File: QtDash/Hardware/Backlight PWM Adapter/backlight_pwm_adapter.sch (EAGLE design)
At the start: 9 parts, among them Q1 310mA/60V/1.6Ω, Q2 310mA/60V/1.6Ω

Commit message: topic/backlight-pwm-control: 	- changed PWM frequency to 30kHz 	- renamed pwm.hpp -> pwm.h 	- started on rev b of PWM adapter board -- pwm signal used directly on EN pin of the OCX OC6700.  There is brightness control that is done outside of the backlight as well that I can't control with the PWM alone.
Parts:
- added C1: 100n, digital_dash:CL10B104MB8NNNC
- added C2: 1u, digital_dash:CL10A105KA8NNNC
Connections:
- net 5V: now also C1.1, C2.1
- net GND: now also C1.2, C2.2
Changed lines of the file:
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@@
 <setting verticaltext="up"/>
 </settings>
-<grid distance="0.1" unitdist="inch" unit="inch" style="lines" multiple="1" display="no" altdistance="0.01" altunitdist="inch" altunit="inch"/>
+<grid distance="0.05" unitdist="inch" unit="inch" style="lines" multiple="1" display="no" altdistance="0.01" altunitdist="inch" altunit="inch"/>
 <layers>
 <layer number="1" name="Top" color="4" fill="1" visible="no" active="no"/>
@@
 <part name="R3" library="digital_dash" deviceset="RC0603JR" device="" technology="-071KL" value="1k"/>
 <part name="GND4" library="SparkFun-PowerSymbols" deviceset="GND" device=""/>
+<part name="C1" library="digital_dash" deviceset="CL" device="" technology="10B104MB8NNNC" value="100n"/>
+<part name="C2" library="digital_dash" deviceset="CL" device="" technology="10A105KA8NNNC" value="1u"/>
+<part name="SUPPLY7" library="SparkFun-PowerSymbols" deviceset="5V" device=""/>
+<part name="GND5" library="SparkFun-PowerSymbols" deviceset="GND" device=""/>
 </parts>
 <sheets>
@@
 <instance part="R3" gate="G$1" x="50.8" y="30.48" rot="R180"/>
 <instance part="GND4" gate="1" x="40.64" y="22.86"/>
+<instance part="C1" gate="G$1" x="72.39" y="78.74"/>
+<instance part="C2" gate="G$1" x="64.77" y="78.74"/>
+<instance part="SUPPLY7" gate="G$1" x="68.58" y="87.63"/>
+<instance part="GND5" gate="1" x="68.58" y="68.58"/>
 </instances>
 <busses>
@@
 <wire x1="43.18" y1="66.04" x2="40.64" y2="66.04" width="0.1524" layer="91"/>
 </segment>
+<segment>
+<pinref part="C2" gate="G$1" pin="2"/>
+<wire x1="64.77" y1="76.2" x2="64.77" y2="73.66" width="0.1524" layer="91"/>
+<pinref part="C1" gate="G$1" pin="2"/>
+<wire x1="64.77" y1="73.66" x2="68.58" y2="73.66" width="0.1524" layer="91"/>
+<wire x1="68.58" y1="73.66" x2="72.39" y2="73.66" width="0.1524" layer="91"/>
+<wire x1="72.39" y1="73.66" x2="72.39" y2="76.2" width="0.1524" layer="91"/>
+<wire x1="68.58" y1="73.66" x2="68.58" y2="71.12" width="0.1524" layer="91"/>
+<junction x="68.58" y="73.66"/>
+<pinref part="GND5" gate="1" pin="GND"/>
+</segment>
 </net>
 <net name="PI_PWM_OUT" class="0">
@@
 <wire x1="119.38" y1="81.28" x2="119.38" y2="86.36" width="0.1524" layer="91"/>
 </segment>
+<segment>
+<pinref part="C2" gate="G$1" pin="1"/>
+<wire x1="64.77" y1="83.82" x2="64.77" y2="85.09" width="0.1524" layer="91"/>
+<pinref part="SUPPLY7" gate="G$1" pin="5V"/>
+<wire x1="64.77" y1="85.09" x2="68.58" y2="85.09" width="0.1524" layer="91"/>
+<wire x1="68.58" y1="85.09" x2="68.58" y2="87.63" width="0.1524" layer="91"/>
+<pinref part="C1" gate="G$1" pin="1"/>
+<wire x1="72.39" y1="83.82" x2="72.39" y2="85.09" width="0.1524" layer="91"/>
+<wire x1="72.39" y1="85.09" x2="68.58" y2="85.09" width="0.1524" layer="91"/>
+<junction x="68.58" y="85.09"/>
+</segment>
 </net>

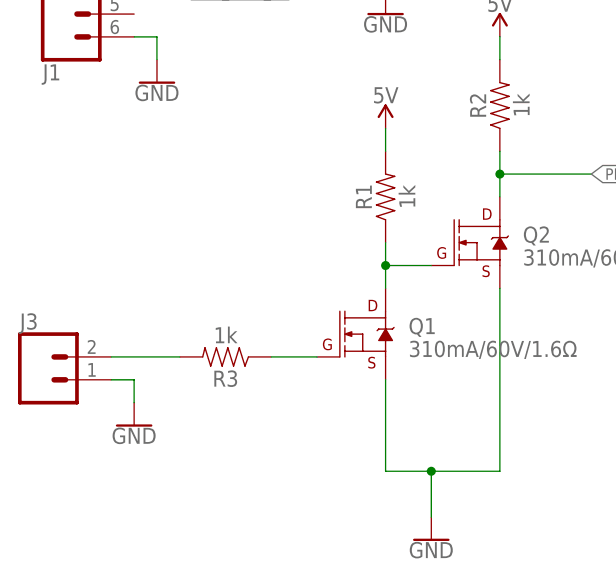
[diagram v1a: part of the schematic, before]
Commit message: topic/backlight-pwm-control: 	- added (weak) pullup on PWM input to PWM adapter board 	- probably just need to make a backlight driver on the main board
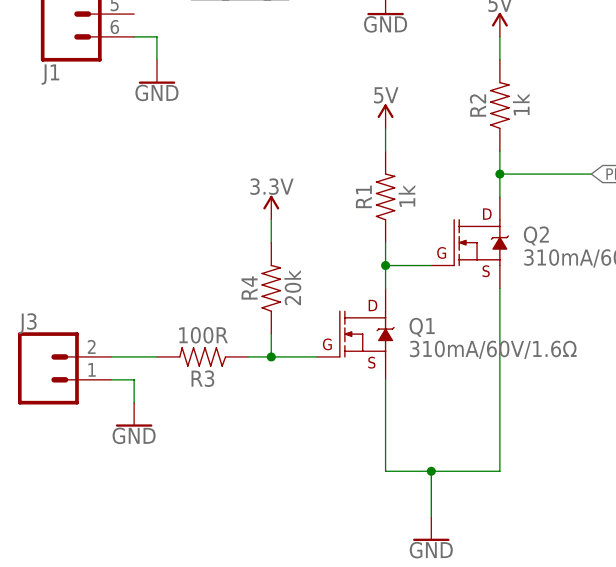
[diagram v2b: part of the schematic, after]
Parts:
- added R4: 20k, digital_dash:RC0603JR-0720KL
- R3: value 1k -> 100R; device digital_dash:RC0603JR-071KL -> digital_dash:RC0603JR-07100RL
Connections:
- net 3.3V: now also R4.2
- net N$2: now also R4.1
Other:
- moved on the sheet: R3
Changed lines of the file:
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@@
 <setting verticaltext="up"/>
 </settings>
-<grid distance="0.05" unitdist="inch" unit="inch" style="lines" multiple="1" display="no" altdistance="0.01" altunitdist="inch" altunit="inch"/>
+<grid distance="0.1" unitdist="inch" unit="inch" style="lines" multiple="1" display="no" altdistance="0.01" altunitdist="inch" altunit="inch"/>
 <layers>
 <layer number="1" name="Top" color="4" fill="1" visible="no" active="no"/>
@@
 <part name="JP1" library="SparkFun-Jumpers" deviceset="JUMPER-SMT_3_NO" device="_SILK"/>
 <part name="J3" library="SparkFun-Connectors" deviceset="CONN_02" device=""/>
-<part name="R3" library="digital_dash" deviceset="RC0603JR" device="" technology="-071KL" value="1k"/>
+<part name="R3" library="digital_dash" deviceset="RC0603JR" device="" technology="-07100RL" value="100R"/>
 <part name="GND4" library="SparkFun-PowerSymbols" deviceset="GND" device=""/>
 <part name="C1" library="digital_dash" deviceset="CL" device="" technology="10B104MB8NNNC" value="100n"/>
@@
 <part name="SUPPLY7" library="SparkFun-PowerSymbols" deviceset="5V" device=""/>
 <part name="GND5" library="SparkFun-PowerSymbols" deviceset="GND" device=""/>
+<part name="R4" library="digital_dash" deviceset="RC0603JR" device="" technology="-0720KL" value="20k"/>
+<part name="SUPPLY8" library="SparkFun-PowerSymbols" deviceset="3.3V" device=""/>
 </parts>
 <sheets>
@@
 <instance part="JP1" gate="G$1" x="78.74" y="116.84" rot="R180"/>
 <instance part="J3" gate="G$1" x="30.48" y="27.94"/>
-<instance part="R3" gate="G$1" x="50.8" y="30.48" rot="R180"/>
+<instance part="R3" gate="G$1" x="48.26" y="30.48" rot="R180"/>
 <instance part="GND4" gate="1" x="40.64" y="22.86"/>
 <instance part="C1" gate="G$1" x="72.39" y="78.74"/>
@@
 <instance part="SUPPLY7" gate="G$1" x="68.58" y="87.63"/>
 <instance part="GND5" gate="1" x="68.58" y="68.58"/>
+<instance part="R4" gate="G$1" x="55.88" y="38.1" rot="R90"/>
+<instance part="SUPPLY8" gate="G$1" x="55.88" y="45.72"/>
 </instances>
 <busses>
@@
 <wire x1="111.76" y1="76.2" x2="111.76" y2="86.36" width="0.1524" layer="91"/>
 </segment>
+<segment>
+<pinref part="R4" gate="G$1" pin="2"/>
+<wire x1="55.88" y1="43.18" x2="55.88" y2="45.72" width="0.1524" layer="91"/>
+<pinref part="SUPPLY8" gate="G$1" pin="3.3V"/>
+</segment>
 </net>
 <net name="LCD_PWM_IN" class="0">
@@
 <pinref part="J3" gate="G$1" pin="2"/>
 <pinref part="R3" gate="G$1" pin="2"/>
-<wire x1="45.72" y1="30.48" x2="38.1" y2="30.48" width="0.1524" layer="91"/>
+<wire x1="43.18" y1="30.48" x2="38.1" y2="30.48" width="0.1524" layer="91"/>
 </segment>
 </net>
@@
 <wire x1="60.96" y1="30.48" x2="55.88" y2="30.48" width="0.1524" layer="91"/>
 <pinref part="R3" gate="G$1" pin="1"/>
-</segment>
-</net>
+<pinref part="R4" gate="G$1" pin="1"/>
+<wire x1="55.88" y1="30.48" x2="53.34" y2="30.48" width="0.1524" layer="91"/>
+<wire x1="55.88" y1="30.48" x2="55.88" y2="33.02" width="0.1524" layer="91"/>
+<junction x="55.88" y="30.48"/>
+</segment>
+</net>

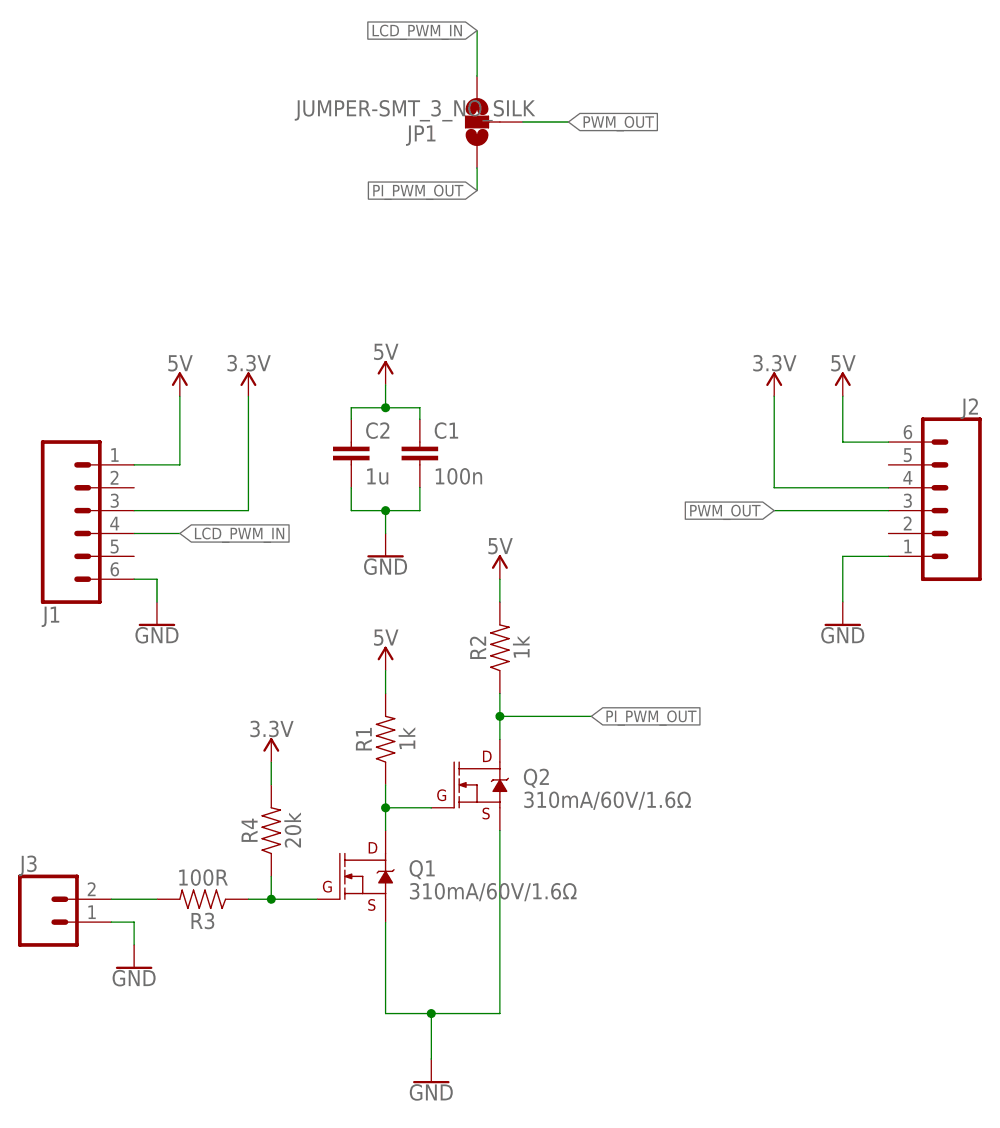
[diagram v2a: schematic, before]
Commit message: topic/hardware-revc: 	- open drain for PWM adapter made non-inverting -- keeps backlight on during boot 	- made use of activeLow backlight config 	- changed backlight initialization values in inittab 	- changed config.ini active low to true
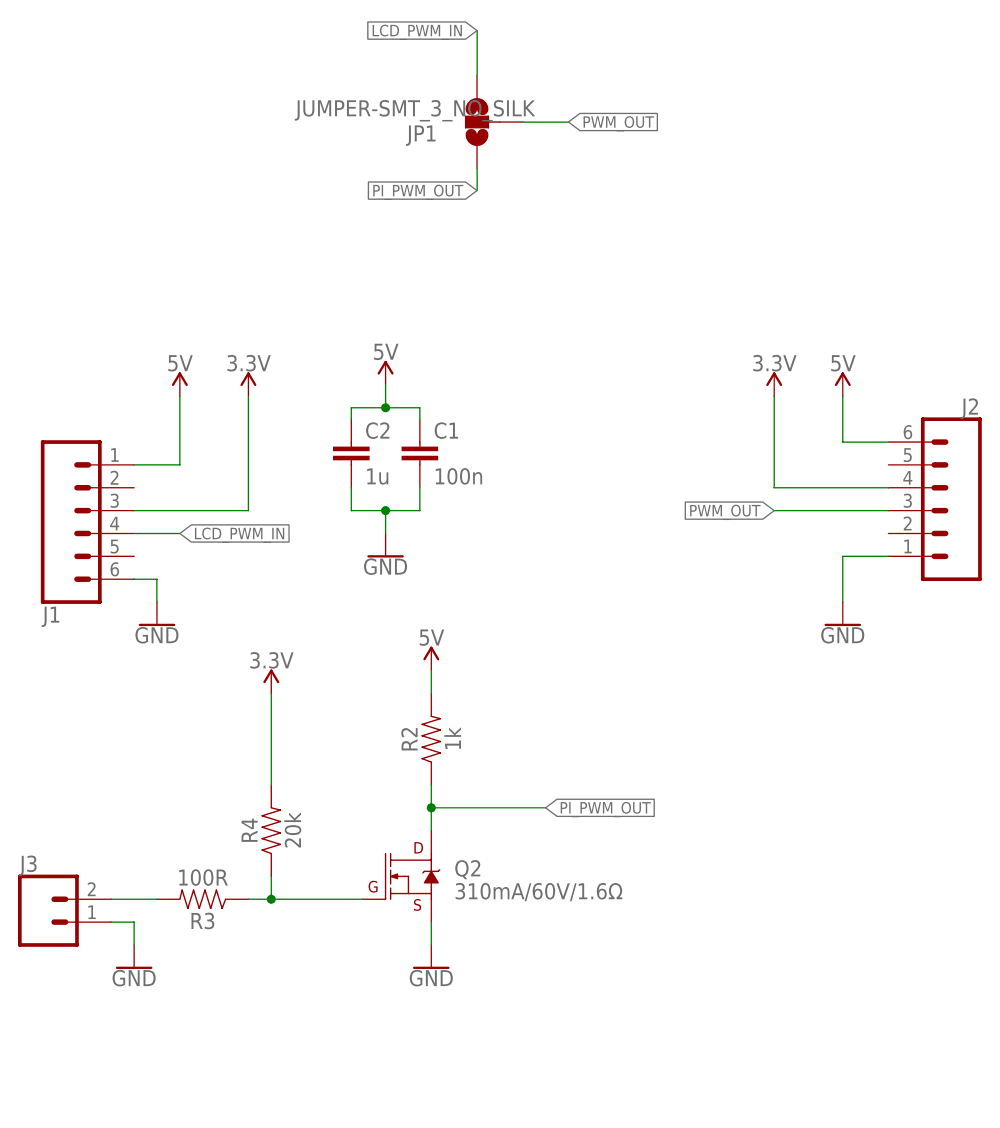
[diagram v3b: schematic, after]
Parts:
- removed Q1: 310mA/60V/1.6Ω, SparkFun-DiscreteSemi:MOSFET-NCH-2N7002PW
- removed R1: 1k, digital_dash:RC0603JR-071KL
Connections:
- removed net N$3: Q1.D, Q2.G, R1.1
- net 5V: no longer R1.2
- net GND: no longer Q1.S
- net N$2: now also Q2.G; no longer Q1.G
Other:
- moved on the sheet: Q2, R2
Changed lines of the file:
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@@
 <part name="SUPPLY3" library="SparkFun-PowerSymbols" deviceset="3.3V" device=""/>
 <part name="SUPPLY4" library="SparkFun-PowerSymbols" deviceset="3.3V" device=""/>
-<part name="Q1" library="SparkFun-DiscreteSemi" deviceset="MOSFET-NCH" device="-2N7002PW" value="310mA/60V/1.6Ω"/>
 <part name="Q2" library="SparkFun-DiscreteSemi" deviceset="MOSFET-NCH" device="-2N7002PW" value="310mA/60V/1.6Ω"/>
-<part name="R1" library="digital_dash" deviceset="RC0603JR" device="" technology="-071KL" value="1k"/>
 <part name="R2" library="digital_dash" deviceset="RC0603JR" device="" technology="-071KL" value="1k"/>
 <part name="GND3" library="SparkFun-PowerSymbols" deviceset="GND" device=""/>
 <part name="SUPPLY5" library="SparkFun-PowerSymbols" deviceset="5V" device=""/>
-<part name="SUPPLY6" library="SparkFun-PowerSymbols" deviceset="5V" device=""/>
 <part name="JP1" library="SparkFun-Jumpers" deviceset="JUMPER-SMT_3_NO" device="_SILK"/>
 <part name="J3" library="SparkFun-Connectors" deviceset="CONN_02" device=""/>
@@
 <instance part="SUPPLY3" gate="G$1" x="53.34" y="86.36"/>
 <instance part="SUPPLY4" gate="G$1" x="111.76" y="86.36"/>
-<instance part="Q1" gate="NMOS" x="66.04" y="33.02"/>
-<instance part="Q2" gate="NMOS" x="78.74" y="43.18"/>
-<instance part="R1" gate="G$1" x="68.58" y="48.26" rot="R90"/>
-<instance part="R2" gate="G$1" x="81.28" y="58.42" rot="R90"/>
-<instance part="GND3" gate="1" x="73.66" y="10.16"/>
-<instance part="SUPPLY5" gate="G$1" x="81.28" y="66.04"/>
-<instance part="SUPPLY6" gate="G$1" x="68.58" y="55.88"/>
+<instance part="Q2" gate="NMOS" x="71.12" y="33.02"/>
+<instance part="R2" gate="G$1" x="73.66" y="48.26" rot="R90"/>
+<instance part="GND3" gate="1" x="73.66" y="22.86"/>
+<instance part="SUPPLY5" gate="G$1" x="73.66" y="55.88"/>
 <instance part="JP1" gate="G$1" x="78.74" y="116.84" rot="R180"/>
 <instance part="J3" gate="G$1" x="30.48" y="27.94"/>
@@
 <instance part="GND5" gate="1" x="68.58" y="68.58"/>
 <instance part="R4" gate="G$1" x="55.88" y="38.1" rot="R90"/>
-<instance part="SUPPLY8" gate="G$1" x="55.88" y="45.72"/>
+<instance part="SUPPLY8" gate="G$1" x="55.88" y="53.34"/>
 </instances>
 <busses>
 </busses>
 <nets>
-<net name="N$3" class="0">
-<segment>
-<pinref part="Q2" gate="NMOS" pin="G"/>
-<pinref part="R1" gate="G$1" pin="1"/>
-<wire x1="73.66" y1="40.64" x2="68.58" y2="40.64" width="0.1524" layer="91"/>
-<wire x1="68.58" y1="40.64" x2="68.58" y2="43.18" width="0.1524" layer="91"/>
-<pinref part="Q1" gate="NMOS" pin="D"/>
-<wire x1="68.58" y1="40.64" x2="68.58" y2="38.1" width="0.1524" layer="91"/>
-<junction x="68.58" y="40.64"/>
-</segment>
-</net>
 <net name="GND" class="0">
 <segment>
-<pinref part="Q1" gate="NMOS" pin="S"/>
-<wire x1="68.58" y1="27.94" x2="68.58" y2="17.78" width="0.1524" layer="91"/>
 <pinref part="Q2" gate="NMOS" pin="S"/>
-<wire x1="81.28" y1="38.1" x2="81.28" y2="17.78" width="0.1524" layer="91"/>
-<wire x1="81.28" y1="17.78" x2="73.66" y2="17.78" width="0.1524" layer="91"/>
-<wire x1="73.66" y1="17.78" x2="68.58" y2="17.78" width="0.1524" layer="91"/>
-<wire x1="73.66" y1="17.78" x2="73.66" y2="12.7" width="0.1524" layer="91"/>
-<junction x="73.66" y="17.78"/>
+<wire x1="73.66" y1="27.94" x2="73.66" y2="25.4" width="0.1524" layer="91"/>
 <pinref part="GND3" gate="1" pin="GND"/>
 </segment>
@@
 <pinref part="Q2" gate="NMOS" pin="D"/>
 <pinref part="R2" gate="G$1" pin="1"/>
-<wire x1="81.28" y1="48.26" x2="81.28" y2="50.8" width="0.1524" layer="91"/>
-<wire x1="81.28" y1="50.8" x2="81.28" y2="53.34" width="0.1524" layer="91"/>
-<wire x1="81.28" y1="50.8" x2="91.44" y2="50.8" width="0.1524" layer="91"/>
-<junction x="81.28" y="50.8"/>
-<label x="91.44" y="50.8" size="1.27" layer="95" xref="yes"/>
+<wire x1="73.66" y1="38.1" x2="73.66" y2="40.64" width="0.1524" layer="91"/>
+<wire x1="73.66" y1="40.64" x2="73.66" y2="43.18" width="0.1524" layer="91"/>
+<wire x1="73.66" y1="40.64" x2="86.36" y2="40.64" width="0.1524" layer="91"/>
+<junction x="73.66" y="40.64"/>
+<label x="86.36" y="40.64" size="1.27" layer="95" xref="yes"/>
 </segment>
 <segment>
@@
 <net name="5V" class="0">
 <segment>
-<pinref part="R1" gate="G$1" pin="2"/>
-<pinref part="SUPPLY6" gate="G$1" pin="5V"/>
-<wire x1="68.58" y1="53.34" x2="68.58" y2="55.88" width="0.1524" layer="91"/>
-</segment>
-<segment>
 <pinref part="R2" gate="G$1" pin="2"/>
 <pinref part="SUPPLY5" gate="G$1" pin="5V"/>
-<wire x1="81.28" y1="63.5" x2="81.28" y2="66.04" width="0.1524" layer="91"/>
+<wire x1="73.66" y1="53.34" x2="73.66" y2="55.88" width="0.1524" layer="91"/>
 </segment>
 <segment>
@@
 <segment>
 <pinref part="R4" gate="G$1" pin="2"/>
-<wire x1="55.88" y1="43.18" x2="55.88" y2="45.72" width="0.1524" layer="91"/>
+<wire x1="55.88" y1="43.18" x2="55.88" y2="53.34" width="0.1524" layer="91"/>
 <pinref part="SUPPLY8" gate="G$1" pin="3.3V"/>
 </segment>
@@
 <net name="N$2" class="0">
 <segment>
-<pinref part="Q1" gate="NMOS" pin="G"/>
-<wire x1="60.96" y1="30.48" x2="55.88" y2="30.48" width="0.1524" layer="91"/>
 <pinref part="R3" gate="G$1" pin="1"/>
 <pinref part="R4" gate="G$1" pin="1"/>
@@
 <wire x1="55.88" y1="30.48" x2="55.88" y2="33.02" width="0.1524" layer="91"/>
 <junction x="55.88" y="30.48"/>
+<pinref part="Q2" gate="NMOS" pin="G"/>
+<wire x1="55.88" y1="30.48" x2="66.04" y2="30.48" width="0.1524" layer="91"/>
 </segment>
 </net>
